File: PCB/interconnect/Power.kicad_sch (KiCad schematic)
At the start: 5 parts, among them Q401 AO3401A, U401 AMS1117

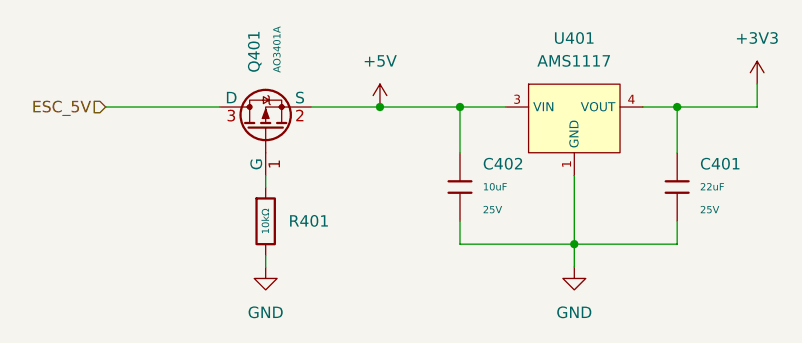
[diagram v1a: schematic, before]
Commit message: Updated PCB, working inference
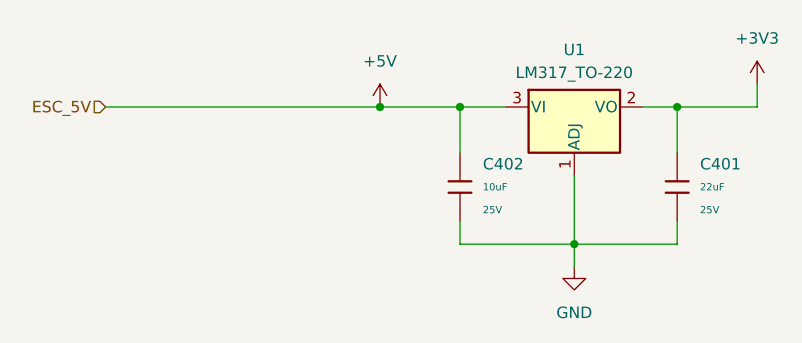
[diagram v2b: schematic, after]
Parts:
- removed Q401: AO3401A, PCM_JLCPCB:Q_SOT-23, symbol PCM_JLCPCB-Transistors:PMOS,AO3401A
- removed R401: 10kΩ, PCM_JLCPCB:R_0805, symbol PCM_JLCPCB-Resistors:0805,10kΩ
- removed U401: AMS1117, PCM_JLCPCB:SOT-223-3_L6.5-W3.4-P2.30-LS7.0-BR, symbol PCM_JLCPCB-Power:LDO, 3.3V, 1A
- added U1: LM317_TO-220, Package_TO_SOT_THT:TO-220-3_Vertical, symbol Regulator_Linear:LM317_TO-220
- C401, C402: footprint PCM_JLCPCB:C_0805 -> Capacitor_THT:C_Disc_D5.0mm_W2.5mm_P2.50mm
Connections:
- net +3V3: now also U1.2 (VO)
- net +5V: now also U1.3 (VI)
- net GND: now also U1.1 (ADJ)
